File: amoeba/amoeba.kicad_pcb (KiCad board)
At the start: 2 copper layers, 18.8 x 16.1 mm, 17 parts

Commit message: Adding net names to amoeba.
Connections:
- net N-000005 renamed /key/led/N-LR0
- net N-000006 renamed /key/switch/N-SD0
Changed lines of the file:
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@@
-(kicad_pcb (version 3) (host pcbnew "(2013-jul-07)-stable")
+(kicad_pcb (version 3) (host pcbnew "(2013-may-18)-stable")
   (general
     (links 18)
@@
     (18 B.Paste user hide)
     (19 F.Paste user hide)
-    (20 B.SilkS user hide)
+    (20 B.SilkS user)
     (21 F.SilkS user hide)
     (22 B.Mask user hide)
@@
     (mod_text_size 1 1)
     (mod_text_width 0.15)
-    (pad_size 1.397 1.397)
-    (pad_drill 0.8128)
+    (pad_size 2.286 2.867377)
+    (pad_drill 1.4986)
     (pad_to_mask_clearance 0)
     (aux_axis_origin 0 0)
-    (visible_elements FFFFFA3F)
+    (visible_elements FFFFB23F)
     (pcbplotparams
       (layerselection 284196865)
@@
   (net 3 /key/SC0)
   (net 4 /key/SR0)
-  (net 5 N-000005)
-  (net 6 N-000006)
+  (net 5 /key/led/N-LR0)
+  (net 6 /key/switch/N-SD0)
   (net_class Default "This is the default net class."
     (clearance 0.254)
@@
     (add_net /key/SC0)
     (add_net /key/SR0)
-    (add_net N-000005)
-    (add_net N-000006)
+    (add_net /key/led/N-LR0)
+    (add_net /key/switch/N-SD0)
   )
   (module RESISTOR (layer B.Cu)
@@
     (pad 1 thru_hole circle (at -5.08 0) (size 1.651 1.651) (drill 0.9906)
       (layers *.Cu *.SilkS *.Mask)
-      (net 5 N-000005)
+      (net 5 /key/led/N-LR0)
     )
     (pad 2 thru_hole circle (at 5.08 0) (size 1.651 1.651) (drill 0.9906)
@@
     (pad 1 thru_hole circle (at -3.81 0) (size 1.397 1.397) (drill 0.8128)
       (layers *.Cu *.Mask B.SilkS)
-      (net 6 N-000006)
+      (net 6 /key/switch/N-SD0)
     )
     (model discret/diode.wrl
@@
     (pad 1 smd rect (at -0.9525 0) (size 0.889 1.397)
       (layers B.Cu B.Paste B.Mask)
-      (net 6 N-000006)
+      (net 6 /key/switch/N-SD0)
     )
     (pad 2 smd rect (at 0.9525 0) (size 0.889 1.397)
@@
     (pad 1 smd rect (at -0.9525 0) (size 0.889 1.397)
       (layers B.Cu B.Paste B.Mask)
-      (net 5 N-000005)
+      (net 5 /key/led/N-LR0)
     )
     (pad 2 smd rect (at 0.9525 0) (size 0.889 1.397)
@@
     (pad 1 thru_hole circle (at -1.27 0) (size 1.6764 1.6764) (drill 0.8128)
       (layers *.Cu *.Mask F.SilkS)
-      (net 5 N-000005)
+      (net 5 /key/led/N-LR0)
     )
     (pad 2 thru_hole circle (at 1.27 0) (size 1.6764 1.6764) (drill 0.8128)
@@
     (pad 1 thru_hole oval (at 2.52 -4.79 356.05481) (size 2.286 2.867377) (drill oval 1.4986 2.079977)
       (layers *.Cu *.SilkS *.Mask)
-      (net 6 N-000006)
+      (net 6 /key/switch/N-SD0)
     )
     (pad 2 thru_hole circle (at -2.5 -4) (size 2.286 2.286) (drill 1.4986)

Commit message: Minor clean-up.
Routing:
- net /key/LR0: track 18.6 -> 17.1 mm
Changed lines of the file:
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@@
     (thickness 1.6)
     (drawings 68)
-    (tracks 103)
+    (tracks 99)
     (zones 0)
     (modules 17)
@@
     (18 B.Paste user hide)
     (19 F.Paste user hide)
-    (20 B.SilkS user)
+    (20 B.SilkS user hide)
     (21 F.SilkS user hide)
     (22 B.Mask user hide)
@@
     (pad_to_mask_clearance 0)
     (aux_axis_origin 0 0)
-    (visible_elements FFFFB23F)
+    (visible_elements FFFFFB3F)
     (pcbplotparams
       (layerselection 284196865)
@@
   (segment (start 244.221 116.84) (end 248.92 116.84) (width 0.254) (layer F.Cu) (net 1))
   (segment (start 242.951 118.11) (end 244.221 116.84) (width 0.254) (layer F.Cu) (net 1))
-  (segment (start 249.8725 113.538) (end 251.333 113.538) (width 0.254) (layer B.Cu) (net 2))
-  (via (at 251.587 113.284) (size 0.889) (layers F.Cu B.Cu) (net 2))
-  (segment (start 251.587 113.284) (end 251.587 114.173) (width 0.254) (layer F.Cu) (net 2))
-  (segment (start 251.333 113.538) (end 251.587 113.284) (width 0.254) (layer B.Cu) (net 2))
+  (segment (start 244.602 114.173) (end 250.444 114.173) (width 0.254) (layer F.Cu) (net 2))
+  (segment (start 243.205 115.57) (end 244.602 114.173) (width 0.254) (layer F.Cu) (net 2))
+  (segment (start 242.57 115.57) (end 243.205 115.57) (width 0.254) (layer F.Cu) (net 2))
+  (segment (start 250.444 114.173) (end 251.333 113.284) (width 0.254) (layer F.Cu) (net 2))
+  (segment (start 254 113.03) (end 251.587 113.03) (width 0.254) (layer F.Cu) (net 2) (status 400000))
+  (segment (start 251.587 113.03) (end 251.333 113.284) (width 0.254) (layer F.Cu) (net 2))
+  (segment (start 249.8725 113.538) (end 251.079 113.538) (width 0.254) (layer B.Cu) (net 2) (status 400000))
+  (segment (start 251.079 113.538) (end 251.333 113.284) (width 0.254) (layer B.Cu) (net 2))
+  (via (at 251.333 113.284) (size 0.889) (layers F.Cu B.Cu) (net 2))
   (segment (start 255.27 115.57) (end 255.27 114.3) (width 0.254) (layer F.Cu) (net 2))
   (segment (start 255.27 114.3) (end 254 113.03) (width 0.254) (layer F.Cu) (net 2))
-  (segment (start 242.57 115.57) (end 243.205 115.57) (width 0.254) (layer F.Cu) (net 2))
-  (segment (start 243.205 115.57) (end 244.602 114.173) (width 0.254) (layer F.Cu) (net 2))
-  (segment (start 244.602 114.173) (end 244.856 114.173) (width 0.254) (layer F.Cu) (net 2))
-  (segment (start 244.856 114.173) (end 251.587 114.173) (width 0.254) (layer F.Cu) (net 2))
-  (segment (start 251.587 114.173) (end 252.857 114.173) (width 0.254) (layer F.Cu) (net 2))
-  (segment (start 252.857 114.173) (end 254 113.03) (width 0.254) (layer F.Cu) (net 2))
-  (segment (start 253.746 113.284) (end 254 113.03) (width 0.254) (layer F.Cu) (net 2))
   (segment (start 243.8654 114.9604) (end 243.8654 114.5794) (width 0.254) (layer B.Cu) (net 3))
   (segment (start 245.11 118.0846) (end 243.8654 116.84) (width 0.254) (layer B.Cu) (net 3))
@@
   (segment (start 242.443 113.538) (end 242.443 109.982) (width 0.254) (layer B.Cu) (net 3))
   (segment (start 245.11 107.95) (end 244.094 107.95) (width 0.254) (layer B.Cu) (net 3))
-  (segment (start 245.11 118.0846) (end 245.11 118.11) (width 0.254) (layer B.Cu) (net 3))
   (segment (start 242.443 113.919) (end 242.443 113.538) (width 0.254) (layer B.Cu) (net 3))
   (segment (start 242.824 114.3) (end 242.443 113.919) (width 0.254) (layer B.Cu) (net 3))
@@
   (segment (start 246.3038 114.4778) (end 245.745 113.919) (width 0.254) (layer B.Cu) (net 4))
   (segment (start 246.3038 116.1288) (end 246.3038 114.4778) (width 0.254) (layer B.Cu) (net 4))
-  (segment (start 251.587 111.76) (end 251.587 112.014) (width 0.254) (layer F.Cu) (net 4))
   (via (at 251.587 111.76) (size 0.889) (layers F.Cu B.Cu) (net 4))
   (segment (start 251.587 111.76) (end 252.476 111.76) (width 0.254) (layer B.Cu) (net 4))

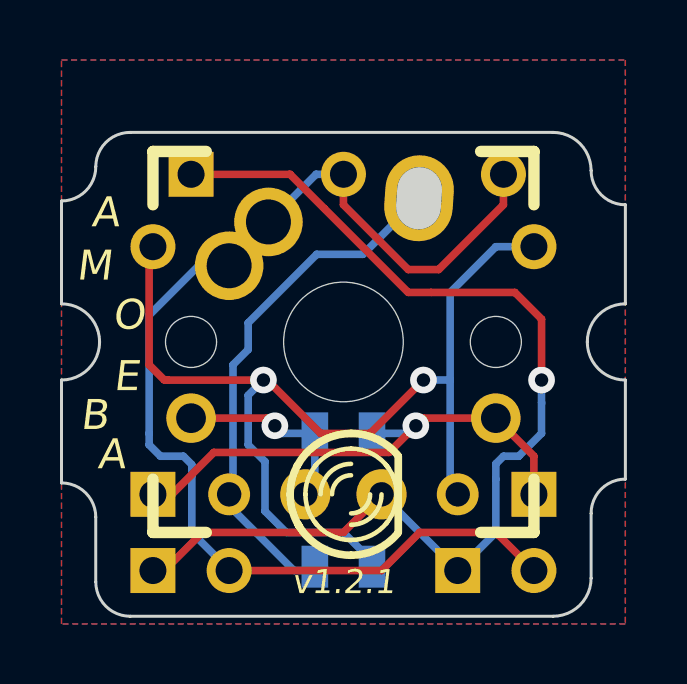
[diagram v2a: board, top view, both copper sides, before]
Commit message: Added DT logo to amoeba.
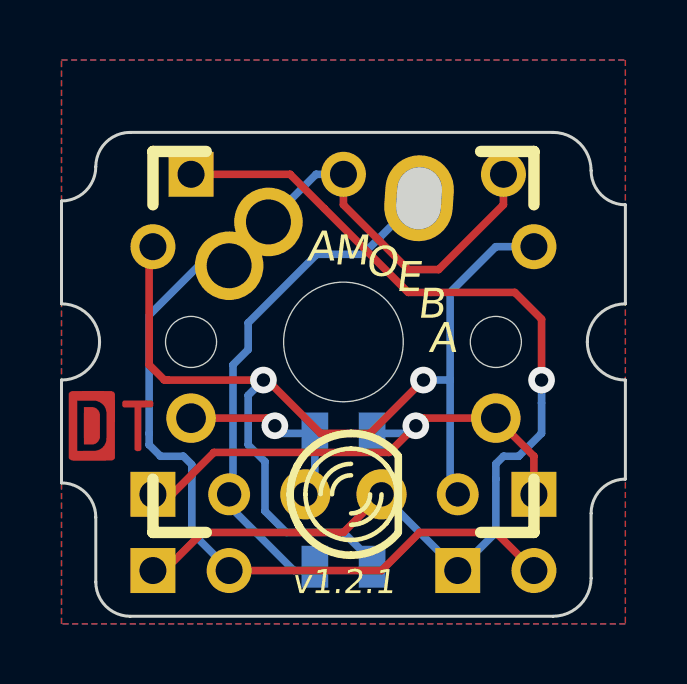
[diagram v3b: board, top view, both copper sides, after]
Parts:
- added G***: DT-Logo, DT-Logo, F.Cu at (241.2, 113.3)

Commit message: Improved DT logos on amoeba.
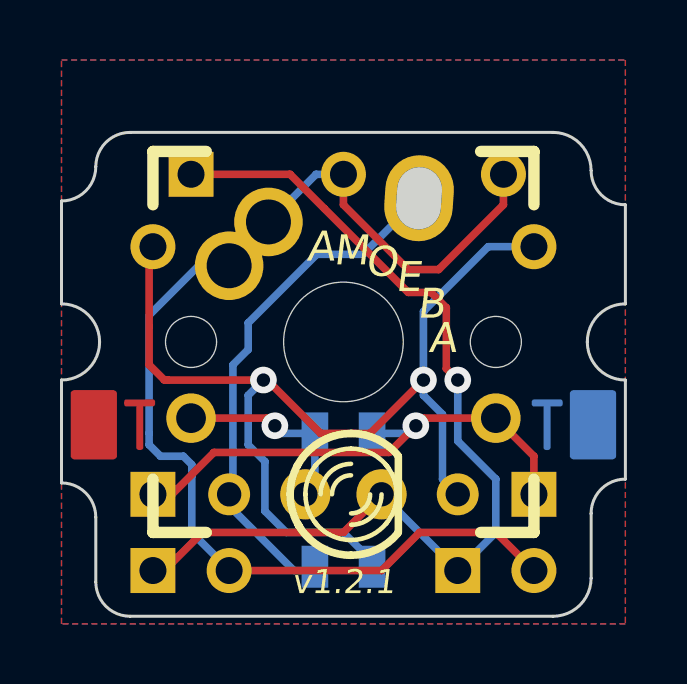
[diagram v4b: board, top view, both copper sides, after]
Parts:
- removed the G*** at (241.2, 113.3)
- added G***: DT-Logo-F.Cu, DT-Logo-F.Cu, F.Cu at (239.3, 111.6)
- added G***: DT-Logo-B.Cu, DT-Logo-B.Cu, F.Cu at (254.6, 111.6)
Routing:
- net /key/LC0: track 35.8 -> 32.6 mm

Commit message: Improvements to DT logo module.
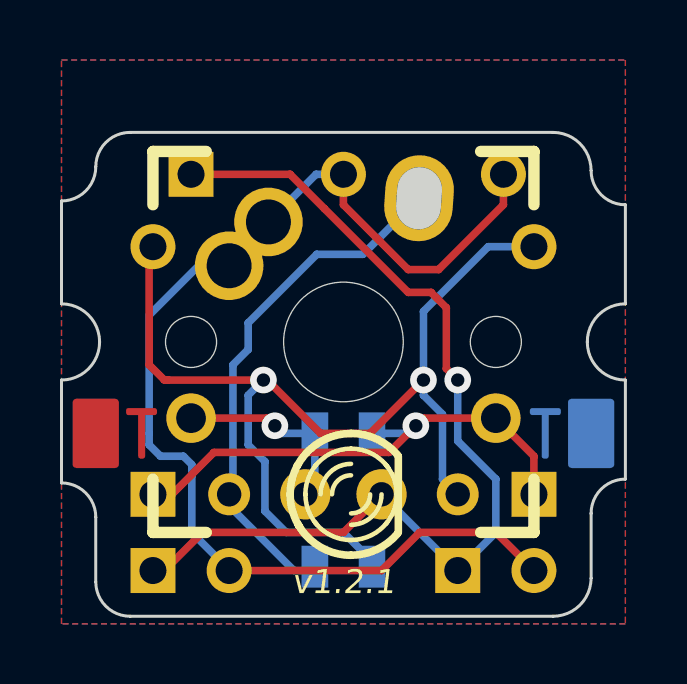
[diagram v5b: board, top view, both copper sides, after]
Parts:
- moved G*** 2.79 mm to (241.3, 113.5)
- moved G*** 2.69 mm to (256.5, 113.5)

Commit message: Added names to silkscreen and copper layers.
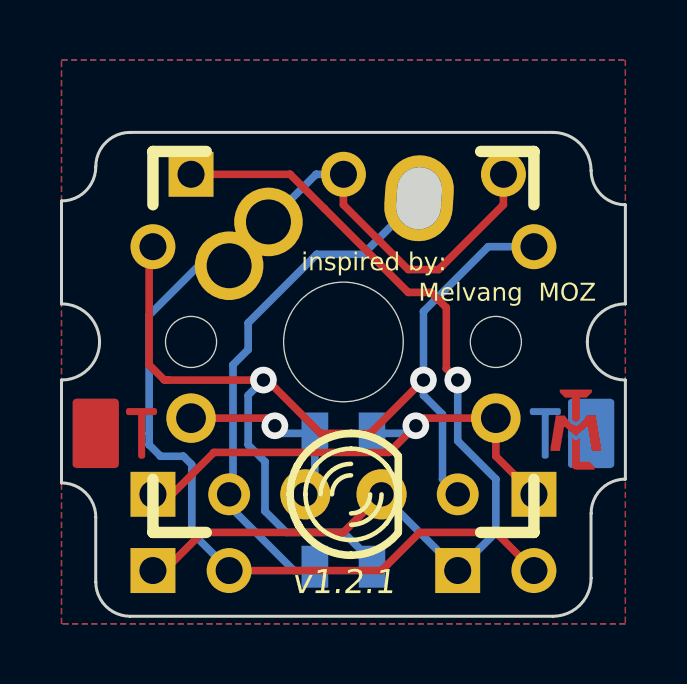
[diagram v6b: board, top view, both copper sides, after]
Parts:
- added mtl-f***: MTL-Sig-F.Cu, MTL-Sig-F.Cu, F.Cu at (256.7, 113.4)
- renumbered G*** to dt-b***, G*** to dt-f***
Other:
- board text added: "Melvang MOZ"
- board text added: "inspired by:"
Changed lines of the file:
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@@
     (links 18)
     (no_connects 1)
-    (area 230.7336 96.366 267.1064 120.218201)
+    (area 230.7336 96.366 267.2334 120.218201)
     (thickness 1.6)
-    (drawings 72)
+    (drawings 75)
     (tracks 97)
     (zones 0)
-    (modules 19)
+    (modules 20)
     (nets 7)
   )
@@
     (18 B.Paste user hide)
     (19 F.Paste user hide)
-    (20 B.SilkS user)
+    (20 B.SilkS user hide)
     (21 F.SilkS user)
     (22 B.Mask user hide)
@@
   (module DT-Logo-B.Cu (layer F.Cu)
     (at 256.54 113.538)
-    (fp_text reference G*** (at 0 3.81) (layer F.SilkS) hide
+    (fp_text reference dt-b*** (at 0 3.81) (layer F.SilkS) hide
       (effects (font (size 1.524 1.524) (thickness 0.3048)))
     )
@@
   (module DT-Logo-F.Cu (layer F.Cu)
     (at 241.3 113.538)
-    (fp_text reference G*** (at 0 3.81) (layer F.SilkS) hide
+    (fp_text reference dt-f*** (at 0 3.81) (layer F.SilkS) hide
       (effects (font (size 1.524 1.524) (thickness 0.3048)))
     )
@@
       (xy 1.33858 -0.84074) (xy 0.43942 -0.84074)) (layer F.Cu) (width 0.00254))
   )
+  (module MTL-Sig-F.Cu (layer F.Cu)
+    (at 256.667 113.411)
+    (fp_text reference mtl-f*** (at 0 3.81) (layer F.SilkS) hide
+      (effects (font (size 1.524 1.524) (thickness 0.3048)))
+    )
+    (fp_text value MTL-Sig-F.Cu (at 0 -3.81) (layer F.SilkS) hide
+      (effects (font (size 1.524 1.524) (thickness 0.3048)))
+    )
+    (fp_poly (pts (xy -1.2446 1.73228) (xy 1.2446 1.73228) (xy 1.2446 -1.73228) (xy -1.2446 -1.73228)
+      (xy -1.2446 1.73228)) (layer F.Mask) (width 0.00254))
+    (fp_poly (pts (xy -0.13208 0.2667) (xy -0.13208 1.19888) (xy -0.12954 1.22428) (xy -0.12192 1.24968)
+      (xy -0.10922 1.27254) (xy -0.09398 1.29286) (xy -0.07366 1.31064) (xy -0.0508 1.32334)
+      (xy -0.0254 1.33096) (xy 0 1.3335) (xy 0.6223 1.3335) (xy 0.6223 1.2446)
+      (xy 0.4445 1.0668) (xy 0.13208 1.0668) (xy 0.13208 0.2667) (xy 0.04318 0.3556)
+      (xy -0.04318 0.3556) (xy -0.13208 0.2667)) (layer F.Cu) (width 0.00254))
+    (fp_poly (pts (xy -0.5334 -1.33096) (xy -0.5334 -1.24206) (xy -0.3556 -1.06426) (xy -0.13208 -1.06426)
+      (xy -0.13208 -0.39878) (xy -0.12954 -0.37338) (xy -0.12192 -0.34798) (xy -0.10922 -0.32258)
+      (xy -0.09398 -0.30226) (xy -0.07366 -0.28702) (xy -0.0508 -0.27432) (xy -0.0254 -0.2667)
+      (xy 0 -0.26416) (xy 0.0254 -0.2667) (xy 0.0508 -0.27432) (xy 0.07366 -0.28702)
+      (xy 0.09398 -0.30226) (xy 0.10922 -0.32258) (xy 0.12192 -0.34798) (xy 0.12954 -0.37338)
+      (xy 0.13208 -0.39878) (xy 0.13208 -1.06426) (xy 0.3556 -1.06426) (xy 0.5334 -1.24206)
+      (xy 0.5334 -1.33096) (xy -0.5334 -1.33096)) (layer F.Cu) (width 0.00254))
+    (fp_poly (pts (xy -0.66548 -0.4699) (xy -0.84328 0.6223) (xy -0.84328 0.7112) (xy -0.5334 0.7112)
+      (xy -0.46482 0.30988) (xy -0.39878 -0.08636) (xy -0.3556 -0.08636) (xy 0 0.22098)
+      (xy 0.3556 -0.08636) (xy 0.39878 -0.08636) (xy 0.5334 0.7112) (xy 0.84328 0.7112)
+      (xy 0.84328 0.6223) (xy 0.66548 -0.4699) (xy 0.3683 -0.4699) (xy 0.35814 -0.45466)
+      (xy 0.33274 -0.41656) (xy 0.29464 -0.36322) (xy 0.24638 -0.29972) (xy 0.21844 -0.26924)
+      (xy 0.18796 -0.23876) (xy 0.15748 -0.21082) (xy 0.127 -0.18542) (xy 0.09398 -0.16256)
+      (xy 0.0635 -0.14732) (xy 0.03048 -0.13462) (xy 0 -0.13208) (xy -0.03048 -0.13462)
+      (xy -0.0635 -0.14732) (xy -0.09398 -0.16256) (xy -0.127 -0.18542) (xy -0.15748 -0.21082)
+      (xy -0.18796 -0.23876) (xy -0.21844 -0.26924) (xy -0.24638 -0.29972) (xy -0.29464 -0.36322)
+      (xy -0.33274 -0.41656) (xy -0.35814 -0.45466) (xy -0.3683 -0.4699) (xy -0.66548 -0.4699)) (layer F.Cu) (width 0.00254))
+  )
+  (gr_line (start 255.27 108.839) (end 255.27 108.839) (angle 90) (layer F.SilkS) (width 0.2))
+  (gr_text "inspired by:" (at 249.936 107.823) (layer F.SilkS)
+    (effects (font (size 0.6 0.6) (thickness 0.15)))
+  )
+  (gr_text "Melvang  MOZ" (at 254.381 108.839) (layer F.SilkS)
+    (effects (font (size 0.6 0.6) (thickness 0.15)))
+  )
   (gr_circle (center 264.75 110.5) (end 266 110.5) (layer Cmts.User) (width 0.1))
   (gr_line (start 262.75 112.5) (end 262.75 108.5) (angle 90) (layer Cmts.User) (width 0.1))
@@
     (effects (font (size 1 1) (thickness 0.2) italic) (justify mirror))
   )
-  (gr_text v1.2.1 (at 242.189 112.141 90) (layer B.SilkS)
+  (gr_text v1.2.1 (at 256.921 107.442 90) (layer B.SilkS)
     (effects (font (size 0.8 0.8) (thickness 0.15) italic) (justify mirror))
   )
@@
   (segment (start 244.221 116.84) (end 248.92 116.84) (width 0.254) (layer F.Cu) (net 1))
   (segment (start 242.951 118.11) (end 244.221 116.84) (width 0.254) (layer F.Cu) (net 1))
+  (segment (start 254 113.03) (end 254 114.3) (width 0.254) (layer F.Cu) (net 2))
+  (segment (start 254 114.3) (end 255.27 115.57) (width 0.254) (layer F.Cu) (net 2))
   (segment (start 244.602 114.173) (end 250.444 114.173) (width 0.254) (layer F.Cu) (net 2))
   (segment (start 243.205 115.57) (end 244.602 114.173) (width 0.254) (layer F.Cu) (net 2))
@@
   (segment (start 251.079 113.538) (end 251.333 113.284) (width 0.254) (layer B.Cu) (net 2))
   (via (at 251.333 113.284) (size 0.889) (layers F.Cu B.Cu) (net 2))
-  (segment (start 255.27 115.57) (end 255.27 114.3) (width 0.254) (layer F.Cu) (net 2))
-  (segment (start 255.27 114.3) (end 254 113.03) (width 0.254) (layer F.Cu) (net 2) (status 20))
   (segment (start 243.8654 114.9604) (end 243.8654 114.5794) (width 0.254) (layer B.Cu) (net 3))
   (segment (start 245.11 118.0846) (end 243.8654 116.84) (width 0.254) (layer B.Cu) (net 3))
@@
       )
     )
+  )
+  (zone (net 0) (net_name "") (layer F.Cu) (hatch full 0.508)
+    (connect_pads (clearance 0.508))
+    (min_thickness 0.254)
+    (keepout (tracks allowed) (vias allowed) (copperpour not_allowed))
+    (fill (arc_segments 16) (thermal_gap 0.508) (thermal_bridge_width 0.508))
+    (polygon
+      (pts
+        (xy 255.397 111.633) (xy 257.937 111.633) (xy 257.937 115.189) (xy 255.397 115.189)
+      )
+    )

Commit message: Update amoeba 1u to v1.3.  Remove svg2mod (now kept in a separate repository.
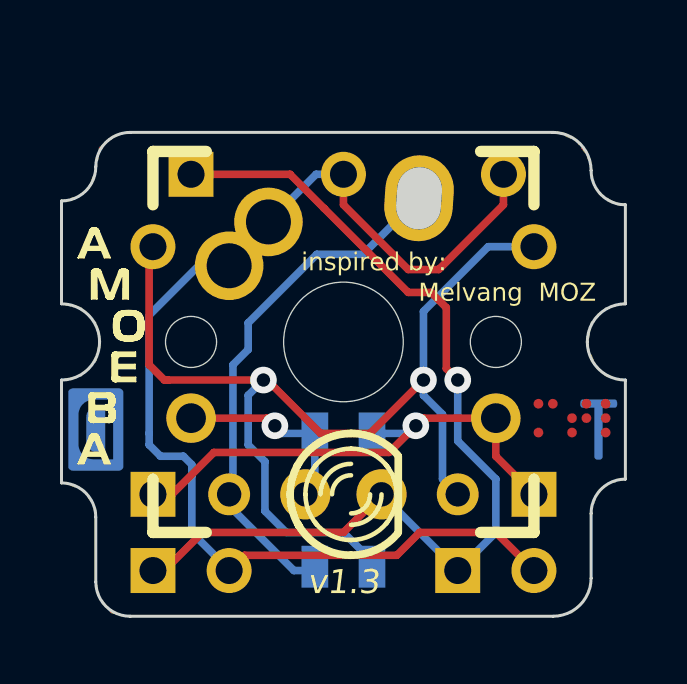
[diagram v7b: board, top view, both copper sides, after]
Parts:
- removed dt-b***: DT-Logo-B.Cu, DT-Logo-B.Cu
- removed dt-f***: DT-Logo-F.Cu, DT-Logo-F.Cu
- removed mtl-f***: MTL-Sig-F.Cu, MTL-Sig-F.Cu
- added DT-Logo-D-Back: G***, DT-Logo-D-Back, F.Cu at (240.7, 113.3)
- added DT-Logo-T-Back: G***, DT-Logo-T-Back, F.Cu at (257.4, 113.4)
- added amoeba-text-round-Back: G***, amoeba-text-round-Back, F.Cu at (248.9, 109.1)
- added amoeba-text-vertical-Front: G***, amoeba-text-vertical-Front, F.Cu at (241.2, 110.6)
- added mtl-braille-Front: G***, mtl-braille-Front, F.Cu at (256.5, 113.0)
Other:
- board text added: "v1.3"
- board text removed: "A"
- board text removed: "B"
- board text removed: "E"
- board text removed: "M"
- board text removed: "O"
- board text removed: "v1.2.1"

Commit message: Updated amoeba PCB with svg modules.
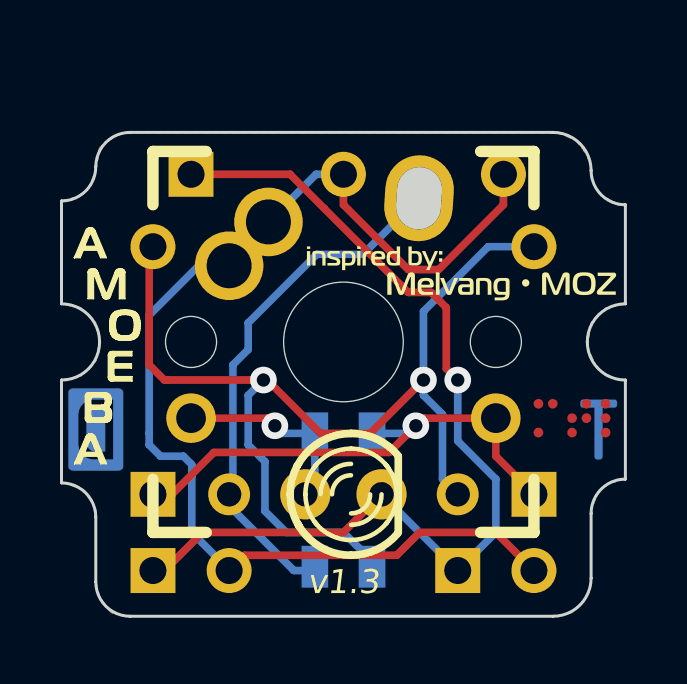
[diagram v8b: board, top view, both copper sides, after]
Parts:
- removed DT-Logo-D-Back: G***, DT-Logo-D-Back
- removed DT-Logo-T-Back: G***, DT-Logo-T-Back
- removed amoeba-text-round-Back: G***, amoeba-text-round-Back
- removed amoeba-text-vertical-Front: G***, amoeba-text-vertical-Front
- removed mtl-braille-Front: G***, mtl-braille-Front
- added amoeba-round-rev: G***, amoeba-round-rev, F.Cu at (248.9, 109.1)
- added amoeba-vertical: G***, amoeba-vertical, F.Cu at (241.0, 110.6)
- added dt-logo-d-rev: G***, dt-logo-d-rev, F.Cu at (240.7, 113.3)
- added dt-logo-t-rev: G***, dt-logo-t-rev, F.Cu at (257.4, 113.4)
- added labels-melvang-moz: G***, labels-melvang-moz, F.Cu at (252.9, 108.2)
- added mtl-braille: G***, mtl-braille, F.Cu at (256.5, 113.0)
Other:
- board text removed: "Melvang MOZ"
- board text removed: "inspired by:"
